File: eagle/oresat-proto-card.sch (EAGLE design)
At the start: 112 parts, among them J1 J-SAMTEC-TFM-110-X1-XXX-D-RA, J2 U.FL, J3 U.FL, J4 U.FL, J6 J-SAMTEC-TFM-120-X1-XXX-D-RA, J7 FTSH-105-XX-X-DV-K, Q1 DMP2240UDM, Q3 MOSFET-PCH-SOT23-6, Q4 MOSFET-PCH-SOT23-6, Q5 PMV45EN, Q6 PMV45EN, U2 TCAN330, U3 MAX7310ATE, U4 MAX4211CETE, U5 TPS62111RSA, U6 STM32F042K6, U7 MCP1703A, X1 16MHZ-2.5x2mm

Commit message: added todo on protocard to connect Iout and Pout to M0
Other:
- note added: "connect Iout and Pout to M0 to monitor power draw"
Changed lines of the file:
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@@
 <?xml version="1.0" encoding="utf-8"?>
 <!DOCTYPE eagle SYSTEM "eagle.dtd">
-<eagle version="9.3.2">
+<eagle version="9.4.0">
 <drawing>
 <settings>
@@
 <text x="170.18" y="114.3" size="1.778" layer="97">47k forces
 slow I2C</text>
+<text x="284.48" y="210.82" size="1.778" layer="100">connect Iout and Pout to
+M0 to monitor power draw</text>
 </plain>
 <instances>

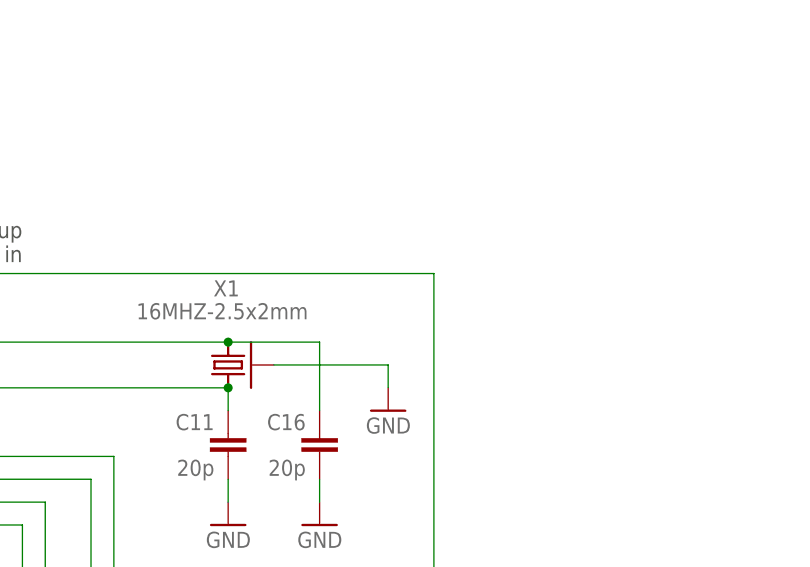
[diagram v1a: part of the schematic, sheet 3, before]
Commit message: added test point on the nreset line
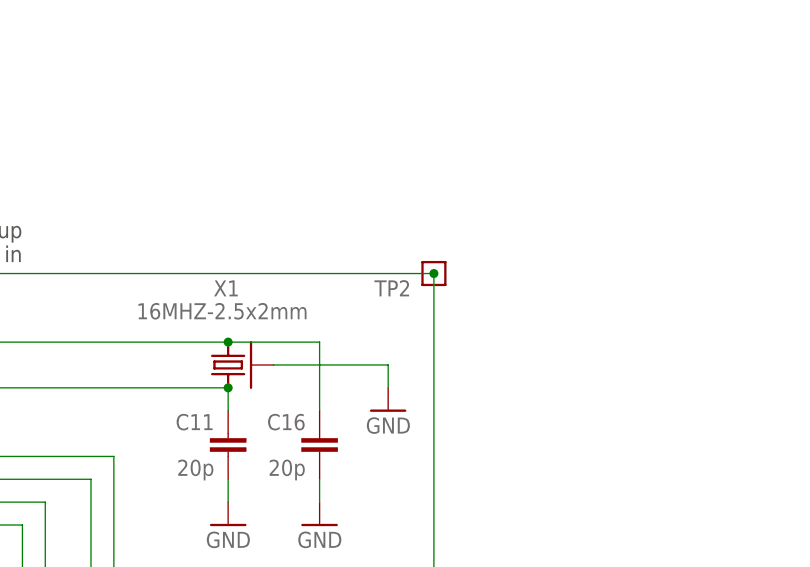
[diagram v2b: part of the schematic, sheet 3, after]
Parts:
- added TP2: TEST-POINT, Tova:TEST-POINT
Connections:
- net NRESET: now also TP2.1
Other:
- note added: "Iout and Pout are analog voltages (0-1.2V) that corresponds to current and power draw respectively"
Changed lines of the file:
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@@
 </part>
 <part name="JP2" library="pinhead" library_urn="urn:adsk.eagle:library:325" deviceset="PINHD-2X5" device="" package3d_urn="urn:adsk.eagle:package:22470/2"/>
+<part name="TP2" library="Tova" deviceset="TEST-POINT" device=""/>
 </parts>
 <sheets>
@@
 <text x="284.48" y="210.82" size="1.778" layer="100">connect Iout and Pout to
 M0 to monitor power draw</text>
+<text x="308.102" y="188.976" size="1.778" layer="97">Iout and Pout are analog voltages (0-1.2V)
+that corresponds to current and power
+draw respectively</text>
 </plain>
 <instances>
@@
 <attribute name="VALUE" x="139.7" y="96.774" size="1.778" layer="96" align="bottom-center"/>
 </instance>
+<instance part="TP2" gate="G$1" x="299.72" y="198.12" smashed="yes" rot="MR0">
+<attribute name="NAME" x="297.18" y="195.58" size="1.778" layer="95" font="vector" rot="MR0"/>
+</instance>
 </instances>
 <busses>
@@
 <pinref part="J7" gate="A" pin="!RESET"/>
 <wire x1="322.58" y1="116.84" x2="299.72" y2="116.84" width="0.1524" layer="91"/>
-</segment>
-</net>
+<pinref part="TP2" gate="G$1" pin="1"/>
+<junction x="299.72" y="198.12"/>
+</segment>
+</net>

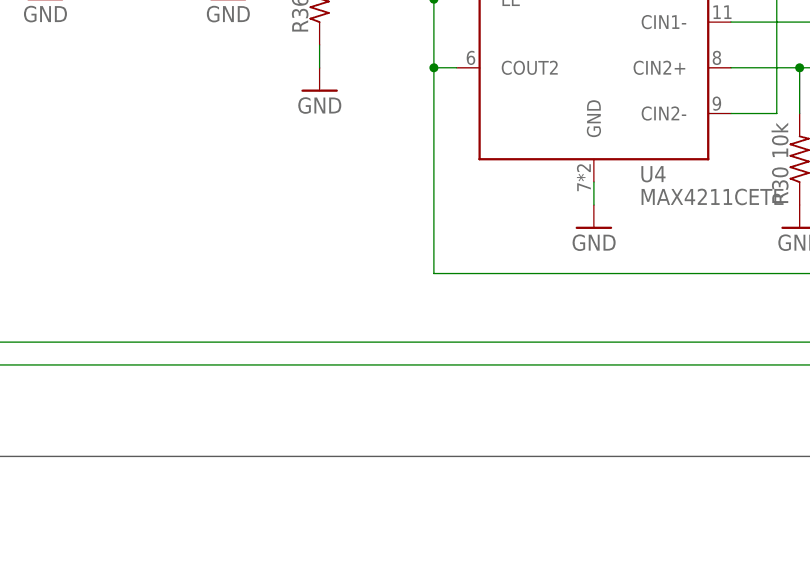
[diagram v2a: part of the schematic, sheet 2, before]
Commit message: added test point to cb_ctrl
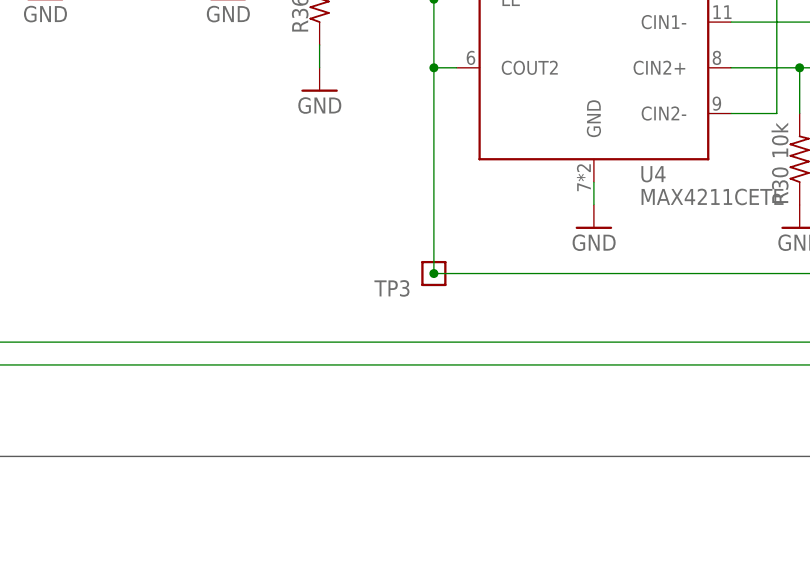
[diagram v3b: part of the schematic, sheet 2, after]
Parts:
- added TP3: TEST-POINT, Tova:TEST-POINT
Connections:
- net CB_CTRL: now also TP3.1
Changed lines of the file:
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@@
 <part name="JP2" library="pinhead" library_urn="urn:adsk.eagle:library:325" deviceset="PINHD-2X5" device="" package3d_urn="urn:adsk.eagle:package:22470/2"/>
 <part name="TP2" library="Tova" deviceset="TEST-POINT" device=""/>
+<part name="TP3" library="Tova" deviceset="TEST-POINT" device=""/>
 </parts>
 <sheets>
@@
 <attribute name="VALUE" x="166.37" y="127" size="1.778" layer="96" rot="R90"/>
 </instance>
+<instance part="TP3" gate="G$1" x="276.86" y="139.7" smashed="yes" rot="MR0">
+<attribute name="NAME" x="274.32" y="137.16" size="1.778" layer="95" font="vector" rot="MR0"/>
+</instance>
 </instances>
 <busses>
@@
 <wire x1="365.76" y1="162.56" x2="363.22" y2="162.56" width="0.1524" layer="91"/>
 <junction x="363.22" y="162.56"/>
-</segment>
-</net>
+<pinref part="TP3" gate="G$1" pin="1"/>
+<junction x="276.86" y="139.7"/>
+</segment>
+</net>

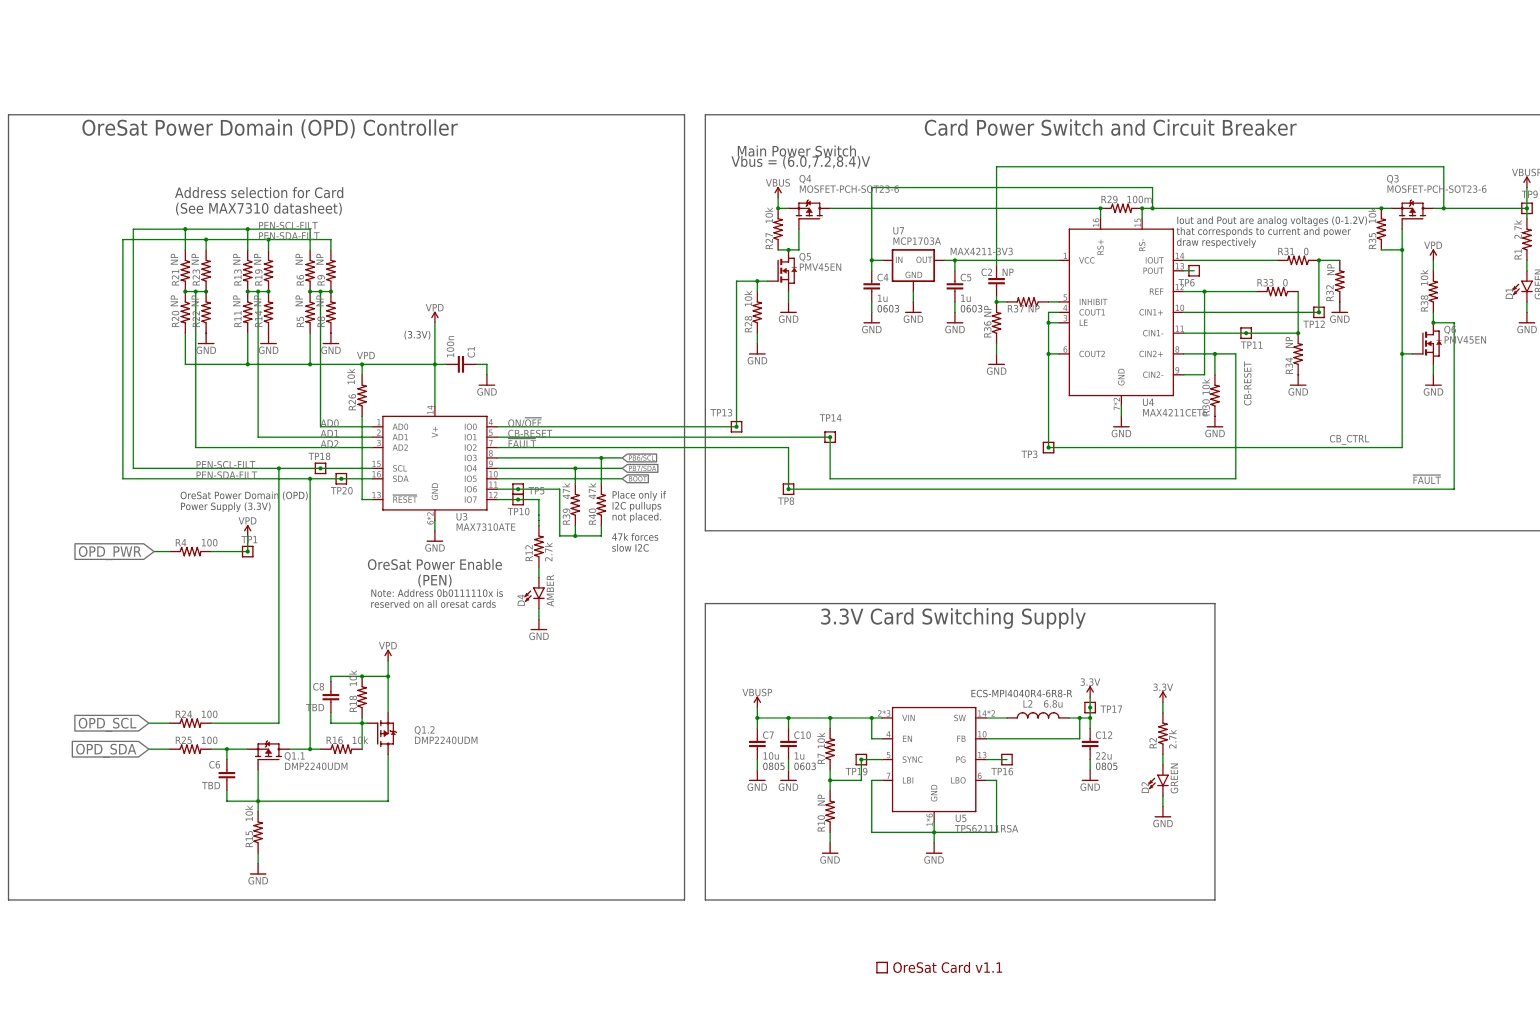
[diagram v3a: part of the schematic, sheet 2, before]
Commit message: updates to OPD, new I2C protection circuit
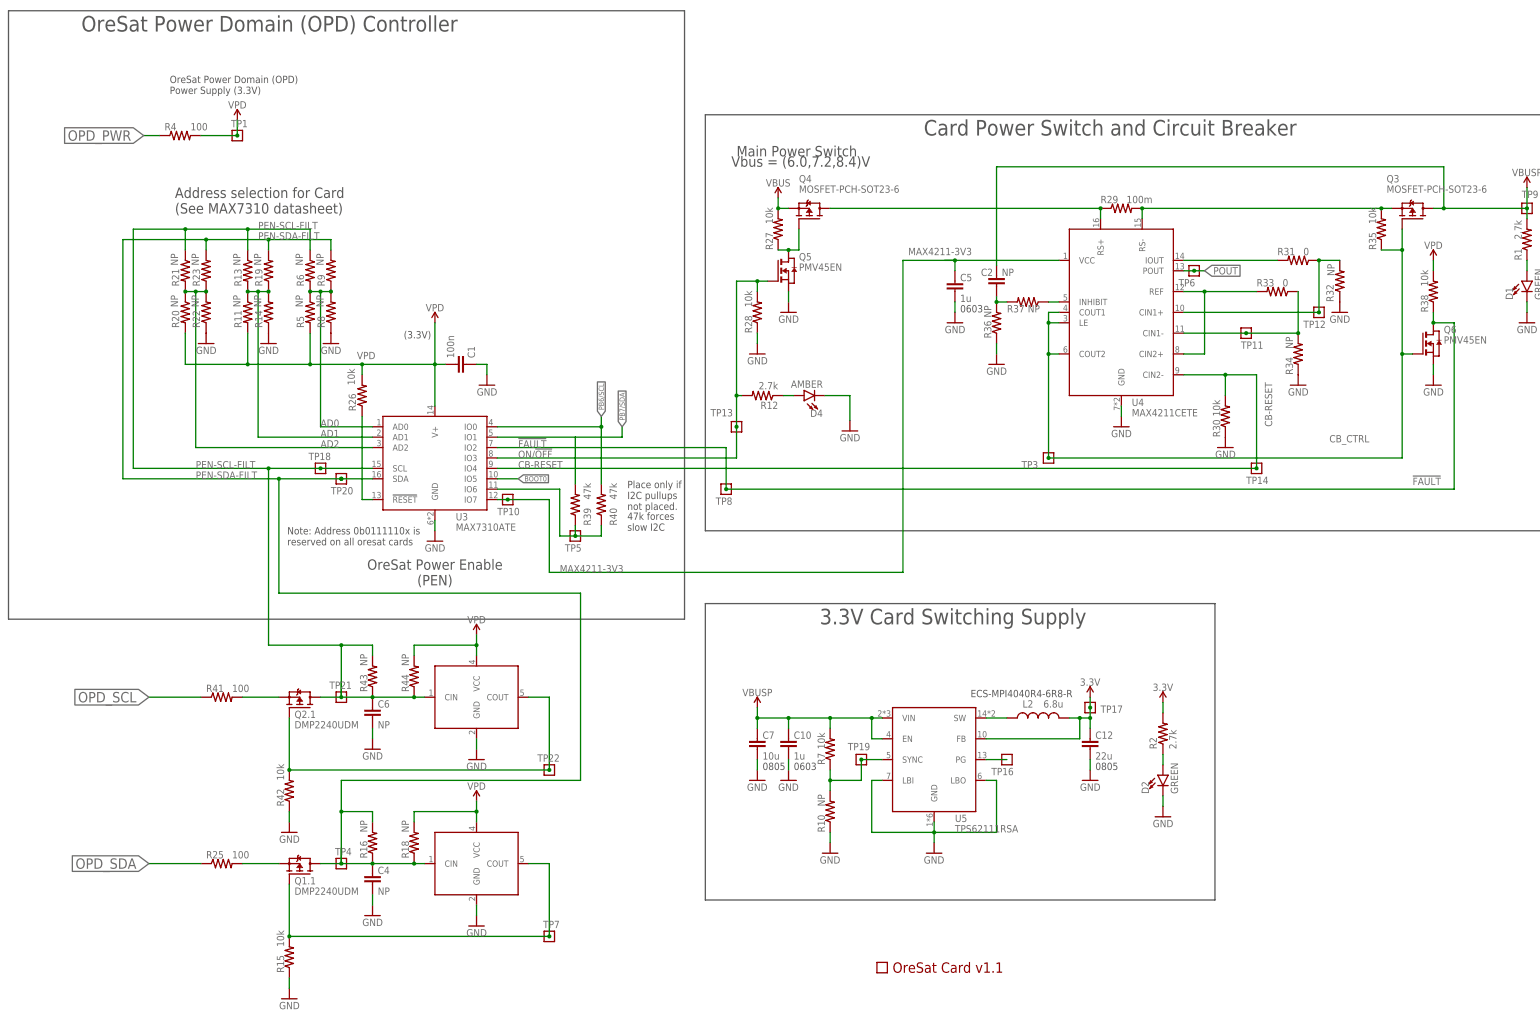
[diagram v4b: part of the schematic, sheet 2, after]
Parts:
- removed C8: TBD, rcl_custom:C-EU0402-B-NOSILK
- removed U7: MCP1703A, v-reg:XC63FPM
- added Q2: DMP2240UDM, Q-MOSFET-PCH-dual-SOT23-6:MOSFET-PCH-SOT23-6
- added R41: 100, rcl_custom:R-US_0402-B-NOSILK
- added R42: 10k, rcl_custom:R-US_0402-B-NOSILK
- added R43, R44: NP, rcl_custom:R-US_0402-B-NOSILK
- added TP21, TP22, TP4, TP7: TEST-POINT, Tova:TEST-POINT
- added U$2, U$3: MIC842, Q-Microchip-MIC842-Comparator:MIC842
- C4: value 1u -> NP; device oresat-rcl:C-EU0603-B-NOSILK -> oresat-rcl:C-EU0805-B-NOSILK; DIS Digi-Key -> (none); DPN 1276-1001-1-ND -> (none); MFR Samsung -> (none); MPN CL05B104KO5NNNC -> (none)
- C6: value TBD -> NP; device rcl_custom:C-EU0402-B-NOSILK -> oresat-rcl:C-EU0805-B-NOSILK; DIS Digi-Key -> (none); DPN 1276-1001-1-ND -> (none); MFR Samsung -> (none); MPN CL05B104KO5NNNC -> (none)
- R16, R18: value 10k -> NP
- R24: value 100 -> 10k; device rcl_custom:R-US_0402-B-NOSILK -> rcl:R-US_R0402; DIS Digi-Key -> (none); DPN 1276-4275-1-ND -> (none); MFR Samsung -> (none); MPN RC1005F6653CS -> (none)
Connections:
- net BOOT renamed BOOT0
- removed net N$573: R12.2, TP10.1, U3.IO7
- removed net N$581: C8.2, Q1.2.G, R16.2, R18.1
- removed net N$598: R31.2, U4.IOUT
- removed net N$600: TP6.1, U4.POUT
- removed net PA15: JP4.11, U6.PA15
- removed net PA8: JP4.13, U6.PA8
- new net IOUT: JP4.11, R31.2, U4.IOUT, U6.PA15
- new net N$479: Q2.1.S, R41.2
- new net N$480: Q2.1.G, R42.2, TP22.1, U$3.COUT
- new net POUT: R24.1, TP6.1, U4.POUT
- new net POUTNAM: JP4.13, R24.2, U6.PA8
- net CB-RESET: now also U3.IO4, U4.CIN2-; no longer U3.IO1, U4.CIN2+
- net GND: now also C6.2, R42.1, U$2.GND, U$3.GND; no longer U7.GND
- net MAX4211-3V3: now also TP10.1, U3.IO7; no longer U7.OUT
- net N$398: no longer C4.1, U7.IN
- net N$579: no longer C6.1
- net N$580: now also TP7.1, U$2.COUT; no longer C6.2, Q1.2.D
- net N$599: now also U4.CIN2+; no longer U4.CIN2-
- net ON/!OFF: now also R12.2, U3.IO3; no longer U3.IO0
- net OPD_SCL: now also R41.1; no longer R24.1
- net PB6/SCL: now also U3.IO0; no longer U3.IO3
- net PB7/SDA: now also U3.IO1; no longer U3.IO4
- net PEN-SCL-FILT: now also C6.1, Q2.1.D, R43.1, R43.2, R44.1, TP21.1, U$3.CIN; no longer R24.2
- net PEN-SDA-FILT: now also C4.1, R16.2, R18.1, TP4.1, U$2.CIN
- net VPD: now also R44.2, U$2.VCC, U$3.VCC; no longer C8.1, Q1.2.S
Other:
- note added: "Power/Current draw from OPD."
- note added: "Signal is analog voltage 0-1.2V"
- note removed: "Iout and Pout are analog voltages (0-1.2V) that corresponds to current and power draw respectively"
- moved on the sheet: C4, C6, D4, Q1.1, R12, R15, R16, R18, R25, R30, R4, TP1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

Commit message: Added new I2C protection, connected Pout to M0 through 10k
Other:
- note removed: "connect Iout and Pout to M0 to monitor power draw"
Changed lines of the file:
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@@
 <text x="173.99" y="119.38" size="1.778" layer="97">47k forces
 slow I2C</text>
-<text x="284.48" y="210.82" size="1.778" layer="100">connect Iout and Pout to
-M0 to monitor power draw</text>
 </plain>
 <instances>

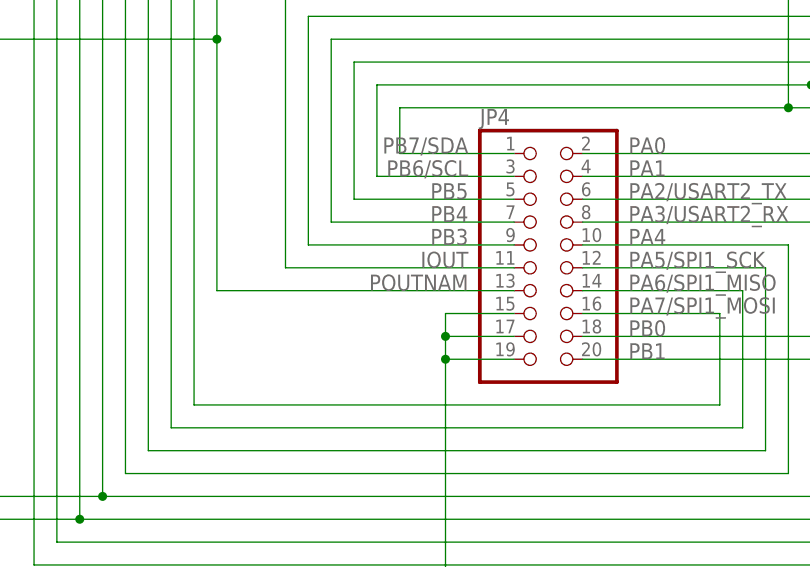
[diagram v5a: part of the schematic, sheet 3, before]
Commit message: added board layout of new I2C protection circuit
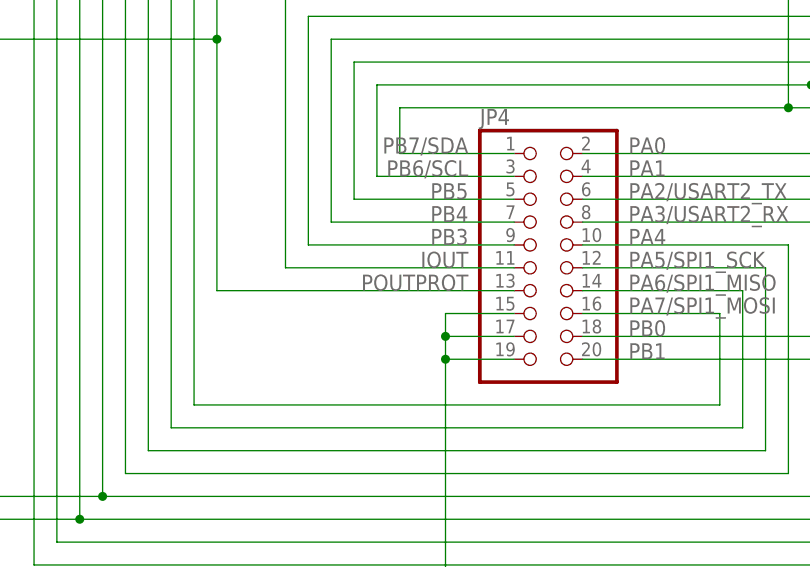
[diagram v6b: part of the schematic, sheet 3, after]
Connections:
- net POUTNAM renamed POUTPROT
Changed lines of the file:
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@@
 </segment>
 </net>
-<net name="POUTNAM" class="0">
+<net name="POUTPROT" class="0">
 <segment>
 <pinref part="U6" gate="G$1" pin="PA8"/>
